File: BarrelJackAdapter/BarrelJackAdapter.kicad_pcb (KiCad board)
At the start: 2 copper layers, 15.2 x 45.7 mm, 7 parts, among them J1 Barrel_Jack_Switch, J2 Conn_01x03, J4 Conn_01x03, U1 L7805

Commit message: wip
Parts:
- added C3: C_P1U, Capacitor_SMD:C_0603_1608Metric, F.Cu at (163.0, 52.1)
- added C4: C_22U_1210, Capacitor_SMD:C_1210_3225Metric, F.Cu at (155.6, 43.2)
- added C5: C_22U_1210, Capacitor_SMD:C_1210_3225Metric, F.Cu at (148.8, 52.9)
- added L1: L_4p7U_13p5A, Inductor_SMD:L_Coilcraft_XxL4040, F.Cu at (155.8, 50.7)
- added R1: R_49p9K, Resistor_SMD:R_0603_1608Metric, F.Cu at (163.0, 54.6)
- added R2: R_10K, Resistor_SMD:R_0603_1608Metric, F.Cu at (163.0, 57.1)
- C1: value 0.33u -> C_10U_805; footprint Capacitor_SMD:C_0603_1608Metric -> Capacitor_SMD:C_0805_2012Metric
- C2: value 0.1u -> C_P1U
- U1: value L7805 -> TPS563207DRLR; footprint Package_TO_SOT_SMD:TO-263-2 -> Package_TO_SOT_SMD:SOT-563
- moved C1 30.5 mm to (153.9, 56.4), turned to -90 degrees
- moved C2 29.2 mm to (163.0, 49.6), turned to 0 degrees
- moved U1 27.8 mm to (158.0, 56.6), turned to 0 degrees
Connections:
- C2 pad 1: +5V -> +9V
- U1 pad 2: GND -> Net-(U1-SW)
- U1 pad 3: +5V -> GND
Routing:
- net GND: vias 66 -> 0
- removed copper zone on F.Cu, net +5V
- removed copper zone on F.Cu, net +9V
- removed copper zone on F.Cu, net GND

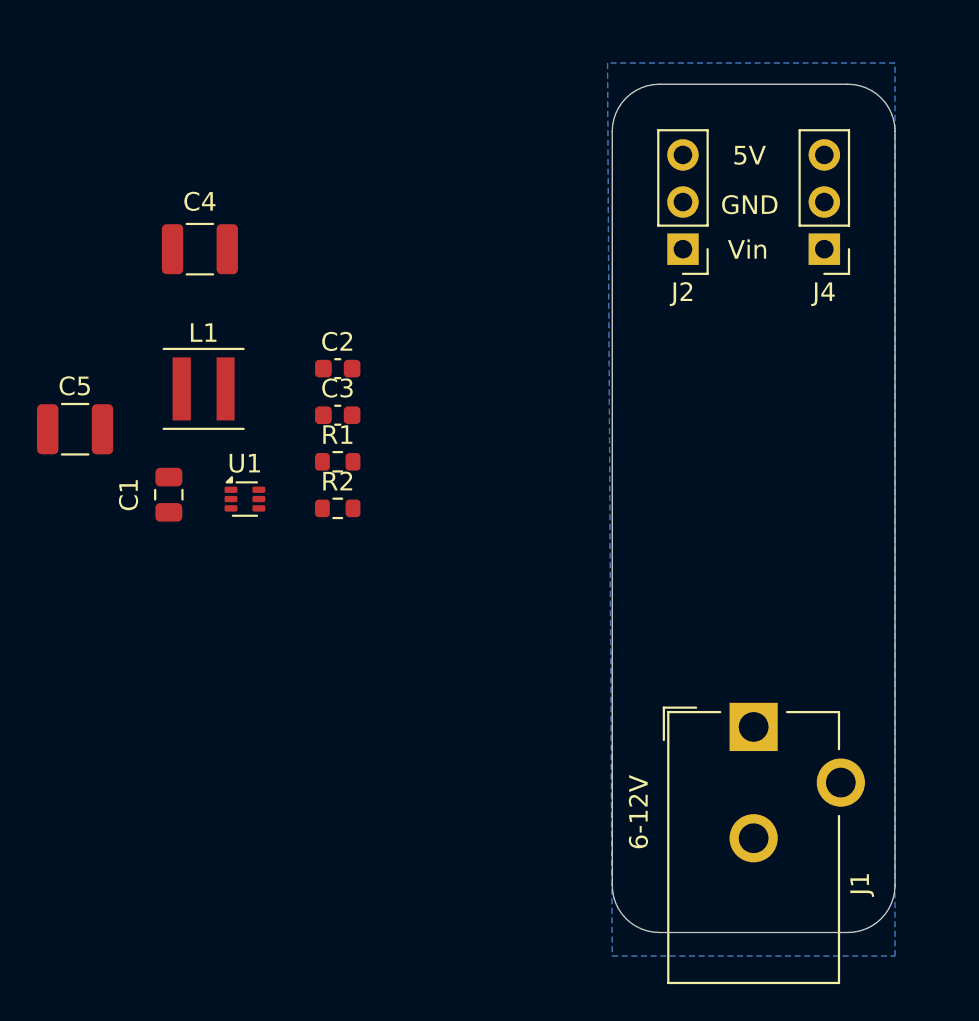
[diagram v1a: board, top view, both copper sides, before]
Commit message: first rev of buck converter based version.
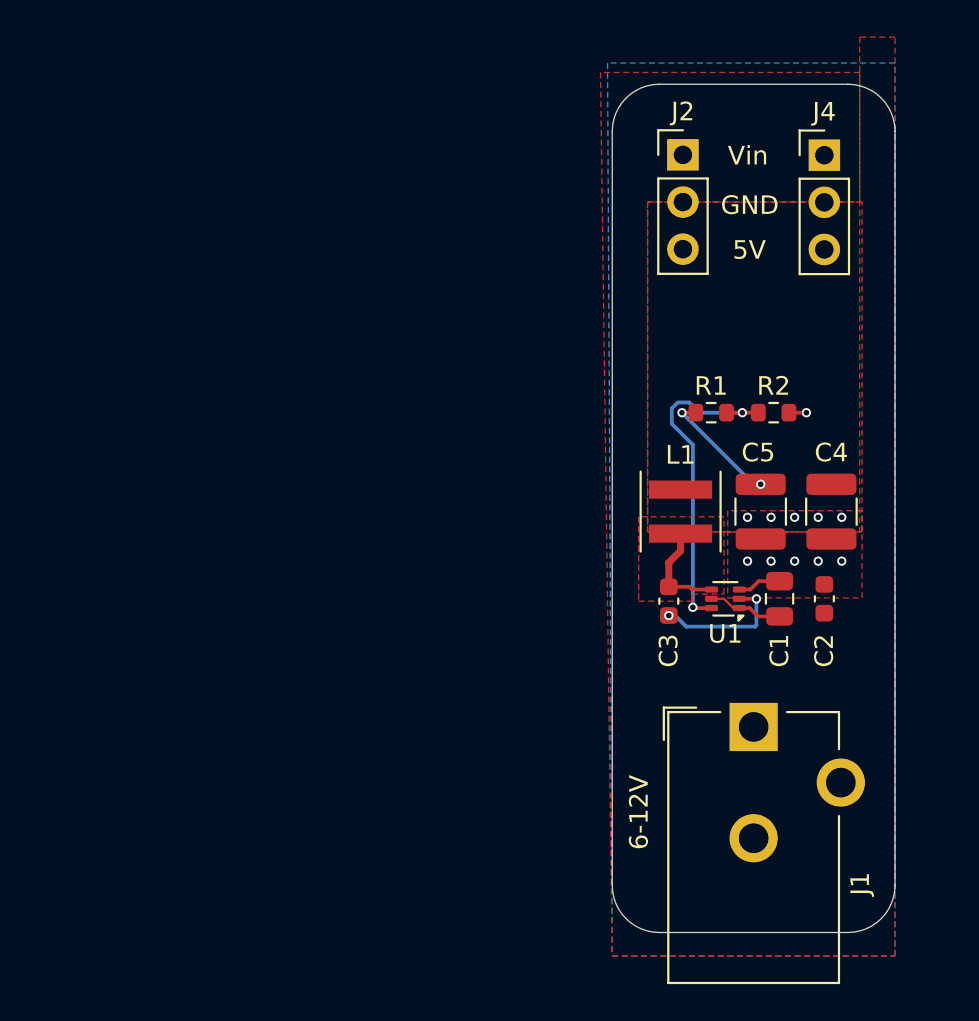
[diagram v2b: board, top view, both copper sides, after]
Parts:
- moved C5 37.2 mm to (185.8, 57.3), turned to -90 degrees
- moved C4 36.9 mm to (189.6, 57.3), turned to -90 degrees
- moved C1 33.4 mm to (186.8, 62.0), turned to 90 degrees
- moved C2 29.0 mm to (189.2, 62.0), turned to 90 degrees
- moved L1 26.5 mm to (181.5, 57.3), turned to 90 degrees
- moved U1 26.4 mm to (183.9, 62.0), turned to 180 degrees
- moved R2 24.1 mm to (186.5, 52.0)
- moved C3 20.5 mm to (180.8, 62.2), turned to -90 degrees
- moved R1 20.3 mm to (183.1, 52.0)
- moved J2 5.08 mm to (181.6, 38.1), turned to 0 degrees
- moved J4 5.06 mm to (189.2, 38.1), turned to 0 degrees
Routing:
- net Net-(U1-FB): track 0.00 -> 18.1 mm, vias 0 -> 2
- net Net-(U1-SW): track 0.00 -> 7.43 mm, vias 0 -> 2
- net +5V: track 0.00 -> 6.59 mm, vias 0 -> 2
- net Net-(U1-BST): track 0.00 -> 5.51 mm
- net +9V: track 0.00 -> 4.06 mm
- net GND: track 0.00 -> 3.30 mm, vias 0 -> 11
- added copper zone on F.Cu, net +5V
- added copper zone on F.Cu, net +9V
- added copper zone on F.Cu, net GND
- added copper zone on F.Cu, net Net-(U1-BST)
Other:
- copper layers 2 -> 4

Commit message: add 3.3v LDO
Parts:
- added C6: C_4p7U, Capacitor_SMD:C_0603_1608Metric, F.Cu at (188.1, 48.8)
- added U2: LDL212PV33R, Package_DFN_QFN:DFN-6-1EP_2x2mm_P0.65mm_EP1x1.6mm, F.Cu at (184.2, 49.1)
- J2, J4: value Conn_01x03 -> Conn_01x04; footprint Connector_PinHeader_2.54mm:PinHeader_1x03_P2.54mm_Vertical -> Connector_PinHeader_2.54mm:PinHeader_1x04_P2.54mm_Vertical
- moved G*** 3.81 mm to (185.4, 53.3)
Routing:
- net +3.3V: track 0.00 -> 16.0 mm
- net +5V: track 6.59 -> 9.84 mm
- net GND: track 3.30 -> 4.28 mm, vias 11 -> 13

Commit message: Remove some vias to the back ground plane.
Localize the high current loop to Front Copper.

Move the switch node connection to Cu2 - sandwich
between clean ground pours.
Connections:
- net Net-(U1-BST) renamed /BST
- net Net-(U1-FB) renamed /FB
- net Net-(U1-SW) renamed /SW
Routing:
- net GND: vias 13 -> 11
- added copper zone on B.Cu, net +9V
- added copper zone on In1.Cu, net GND
- added copper zone on In2.Cu, net GND
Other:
- board text added: "3.3V"
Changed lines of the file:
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@@
 	(net 2 "+9V")
 	(net 3 "+5V")
-	(net 4 "Net-(U1-SW)")
-	(net 5 "Net-(U1-BST)")
-	(net 6 "Net-(U1-FB)")
+	(net 4 "/SW")
+	(net 5 "/BST")
+	(net 6 "/FB")
 	(net 7 "+3.3V")
 	(net 8 "unconnected-(U2-NC-Pad5)")
@@
 			(layers "F.Cu" "F.Paste" "F.Mask")
 			(roundrect_rratio 0.25)
-			(net 4 "Net-(U1-SW)")
+			(net 4 "/SW")
 			(pinfunction "SW")
 			(pintype "output")
@@
 			(layers "F.Cu" "F.Paste" "F.Mask")
 			(roundrect_rratio 0.25)
-			(net 5 "Net-(U1-BST)")
+			(net 5 "/BST")
 			(pinfunction "BST")
 			(pintype "output")
@@
 			(layers "F.Cu" "F.Paste" "F.Mask")
 			(roundrect_rratio 0.25)
-			(net 6 "Net-(U1-FB)")
+			(net 6 "/FB")
 			(pinfunction "FB")
 			(pintype "input")
@@
 		(tags "DFN 0.65")
 		(property "Reference" "U2"
-			(at 3.302 -0.146 360)
+			(at 3.302 -0.146 0)
 			(layer "F.SilkS")
 			(effects
@@
 		)
 		(property "Value" "LDL212PV33R"
-			(at 0 2.025 360)
+			(at 0 2.025 0)
 			(layer "F.Fab")
 			(effects
@@
 		)
 		(fp_text user "${REFERENCE}"
-			(at 0 0 360)
+			(at 0 0 0)
 			(layer "F.Fab")
 			(effects
@@
 			(layers "F.Cu" "F.Paste" "F.Mask")
 			(roundrect_rratio 0.25)
-			(net 5 "Net-(U1-BST)")
+			(net 5 "/BST")
 			(pintype "passive")
 		)
@@
 			(layers "F.Cu" "F.Paste" "F.Mask")
 			(roundrect_rratio 0.25)
-			(net 4 "Net-(U1-SW)")
+			(net 4 "/SW")
 			(pintype "passive")
 		)
@@
 			(layers "F.Cu" "F.Paste" "F.Mask")
 			(roundrect_rratio 0.25)
-			(net 6 "Net-(U1-FB)")
+			(net 6 "/FB")
 			(pintype "passive")
 		)
@@
 		(tags "capacitor")
 		(property "Reference" "C6"
-			(at 3.035 0 360)
+			(at 3.035 0 0)
 			(layer "F.SilkS")
 			(effects
@@
 		)
 		(property "Value" "C_4p7U"
-			(at 0 1.43 360)
+			(at 0 1.43 0)
 			(layer "F.Fab")
 			(effects
@@
 		)
 		(fp_text user "${REFERENCE}"
-			(at 0 0 360)
+			(at 0 0 0)
 			(layer "F.Fab")
 			(effects
@@
 			(layers "F.Cu" "F.Paste" "F.Mask")
 			(roundrect_rratio 0.25)
-			(net 6 "Net-(U1-FB)")
+			(net 6 "/FB")
 			(pintype "passive")
 		)
@@
 			(size 0.98 3.4)
 			(layers "F.Cu" "F.Paste" "F.Mask")
-			(net 5 "Net-(U1-BST)")
+			(net 5 "/BST")
 			(pinfunction "1")
 			(pintype "passive")
@@
 		)
 	)
+	(gr_text "3.3V"
+		(at 183.769 46.355 0)
+		(layer "F.SilkS")
+		(effects
+			(font
+				(size 1 1)
+				(thickness 0.15)
+			)
+			(justify left bottom)
+		)
+	)
 	(gr_text "Vin"
 		(at 184.023 38.735 0)
@@
 	)
 	(via
-		(at 186.3598 57.6326)
-		(size 0.5)
-		(drill 0.3)
+		(at 184.15 49.149)
+		(size 0.35)
+		(drill 0.2)
 		(layers "F.Cu" "B.Cu")
-		(free yes)
 		(net 1)
 	)
 	(via
-		(at 188.8998 59.9948)
+		(at 186.3598 57.6326)
 		(size 0.5)
 		(drill 0.3)
@@
 	)
 	(via
-		(at 185.0898 59.9948)
-		(size 0.5)
-		(drill 0.3)
+		(at 184.15 48.641)
+		(size 0.35)
+		(drill 0.2)
 		(layers "F.Cu" "B.Cu")
-		(free yes)
 		(net 1)
 	)
@@
 	)
 	(via
-		(at 186.3598 59.9948)
-		(size 0.5)
-		(drill 0.3)
-		(layers "F.Cu" "B.Cu")
-		(free yes)
-		(net 1)
-	)
-	(via
-		(at 190.1698 59.9948)
-		(size 0.5)
-		(drill 0.3)
-		(layers "F.Cu" "B.Cu")
-		(free yes)
-		(net 1)
-	)
-	(via
 		(at 190.1698 57.6326)
 		(size 0.5)
@@
 	)
 	(via
-		(at 187.6298 59.9948)
+		(at 188.8998 57.6326)
 		(size 0.5)
 		(drill 0.3)
@@
 	)
 	(via
-		(at 188.8998 57.6326)
-		(size 0.5)
-		(drill 0.3)
+		(at 184.15 49.657)
+		(size 0.35)
+		(drill 0.2)
 		(layers "F.Cu" "B.Cu")
-		(free yes)
 		(net 1)
 	)
@@
 		(end 185.801 55.851)
 		(width 0.2)
-		(layer "B.Cu")
+		(layer "In2.Cu")
 		(net 3)
 	)
@@
 		(end 185.4164 55.851)
 		(width 0.2)
-		(layer "B.Cu")
+		(layer "In2.Cu")
 		(net 3)
 	)
@@
 		(end 185.4962 63.5254)
 		(width 0.2)
-		(layer "B.Cu")
+		(layer "In2.Cu")
 		(net 4)
 	)
@@
 		(end 181.7878 63.5254)
 		(width 0.2)
-		(layer "B.Cu")
+		(layer "In2.Cu")
 		(net 4)
 	)
@@
 		(end 185.5724 63.4492)
 		(width 0.2)
-		(layer "B.Cu")
+		(layer "In2.Cu")
 		(net 4)
 	)
@@
 		(end 180.848 62.927)
 		(width 0.2)
-		(layer "B.Cu")
+		(layer "In2.Cu")
 		(net 4)
 	)
@@
 		(end 181.1894 62.927)
 		(width 0.2)
-		(layer "B.Cu")
+		(layer "In2.Cu")
 		(net 4)
 	)
@@
 		(end 181.0092 52.5868)
 		(width 0.2)
-		(layer "B.Cu")
+		(layer "In2.Cu")
 		(net 6)
 	)
@@
 		(end 182.499 51.9938)
 		(width 0.2)
-		(layer "B.Cu")
+		(layer "In2.Cu")
 		(net 6)
 	)
@@
 		(end 181.331382 51.4438)
 		(width 0.2)
-		(layer "B.Cu")
+		(layer "In2.Cu")
 		(net 6)
 	)
@@
 		(end 182.1434 53.721)
 		(width 0.2)
-		(layer "B.Cu")
+		(layer "In2.Cu")
 		(net 6)
 	)
@@
 		(end 181.949 51.4438)
 		(width 0.2)
-		(layer "B.Cu")
+		(layer "In2.Cu")
 		(net 6)
 	)
@@
 		(end 182.0799 53.6575)
 		(width 0.2)
-		(layer "B.Cu")
+		(layer "In2.Cu")
 		(net 6)
 	)
@@
 		(end 182.0926 51.5874)
 		(width 0.2)
-		(layer "B.Cu")
+		(layer "In2.Cu")
 		(net 6)
 	)
@@
 		(end 181.0092 51.765982)
 		(width 0.2)
-		(layer "B.Cu")
+		(layer "In2.Cu")
 		(net 6)
 	)
@@
 		(end 182.0799 53.6575)
 		(width 0.2)
-		(layer "B.Cu")
+		(layer "In2.Cu")
 		(net 6)
 	)
@@
 	)
 	(zone
-		(net 2)
-		(net_name "+9V")
-		(layer "F.Cu")
-		(hatch edge 0.5)
-		(connect_pads thru_hole_only
-			(clearance 0.5)
-		)
-		(min_thickness 0.25)
-		(filled_areas_thickness no)
-		(fill yes
-			(thermal_gap 0.5)
-			(thermal_bridge_width 0.5)
-		)
-		(polygon
-			(pts
-				(xy 191.135 31.75) (xy 191.135 58.42) (xy 179.705 58.42) (xy 179.705 40.64) (xy 191.135 40.64) (xy 191.135 33.655)
-				(xy 177.165 33.655) (xy 177.8 81.28) (xy 193.04 81.28) (xy 193.04 31.75)
-			)
-		)
-	)
-	(zone
 		(net 3)
 		(net_name "+5V")
@@
 		(priority 1)
 		(connect_pads thru_hole_only
-			(clearance 0.5)
+			(clearance 0.25)
 		)
-		(min_thickness 0.25)
+		(min_thickness 0.2)
 		(filled_areas_thickness no)
 		(fill yes
@@
 	(zone
 		(net 5)
-		(net_name "Net-(U1-BST)")
+		(net_name "/BST")
 		(layer "F.Cu")
 		(hatch edge 0.5)
 		(priority 3)
 		(connect_pads thru_hole_only
-			(clearance 0.5)
+			(clearance 0.25)
 		)
-		(min_thickness 0.25)
+		(min_thickness 0.2)
 		(filled_areas_thickness no)
 		(fill yes
@@
 	)
 	(zone
+		(net 2)
+		(net_name "+9V")
+		(layers "F&B.Cu")
+		(hatch edge 0.5)
+		(connect_pads thru_hole_only
+			(clearance 0.25)
+		)
+		(min_thickness 0.2)
+		(filled_areas_thickness no)
+		(fill yes
+			(thermal_gap 0.5)
+			(thermal_bridge_width 0.5)
+		)
+		(polygon
+			(pts
+				(xy 191.135 31.75) (xy 191.135 58.42) (xy 179.705 58.42) (xy 179.705 40.64) (xy 191.135 40.64) (xy 191.135 33.655)
+				(xy 177.165 33.655) (xy 177.8 81.28) (xy 193.04 81.28) (xy 193.04 31.75)
+			)
+		)
+	)
+	(zone
 		(net 1)
 		(net_name "GND")
-		(layer "B.Cu")
+		(layers "In1.Cu" "In2.Cu" "B.Cu")
 		(hatch edge 0.5)
 		(priority 2)

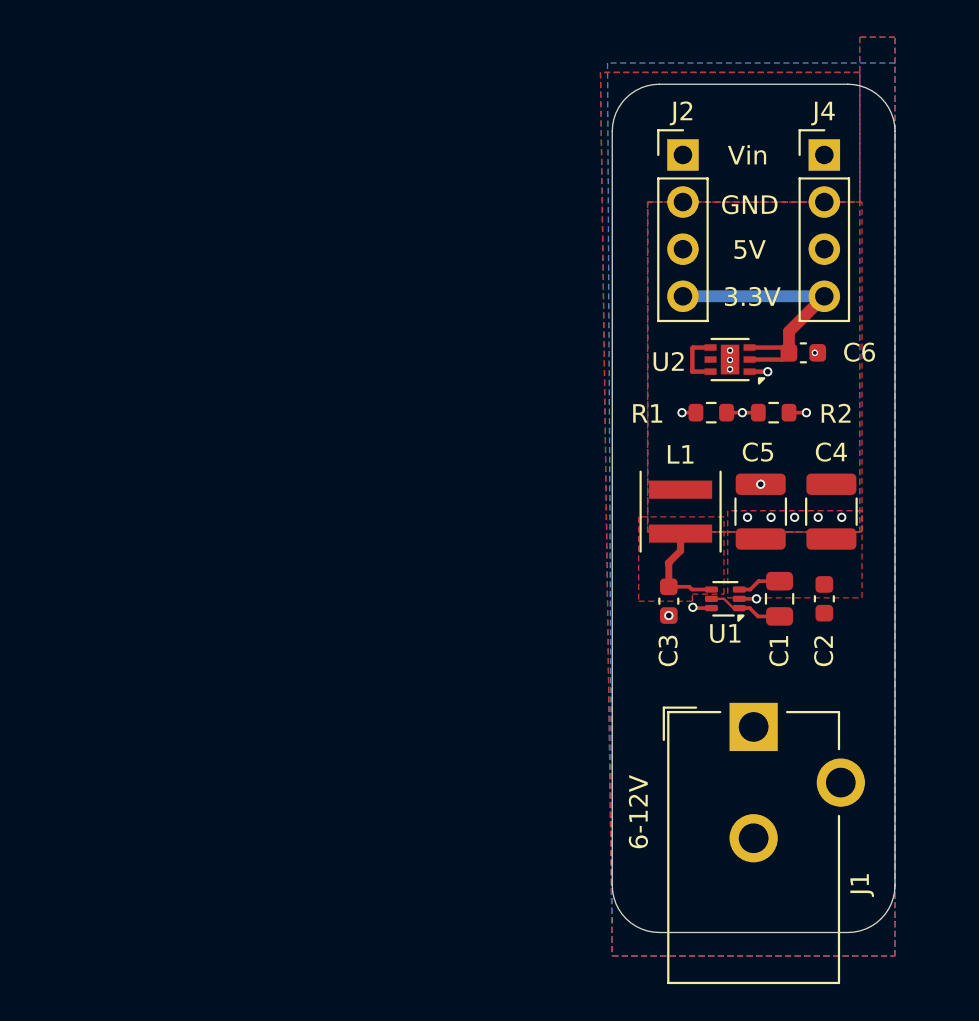
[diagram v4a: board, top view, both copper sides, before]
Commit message: Fix schematic.
Better Layout

Close #2
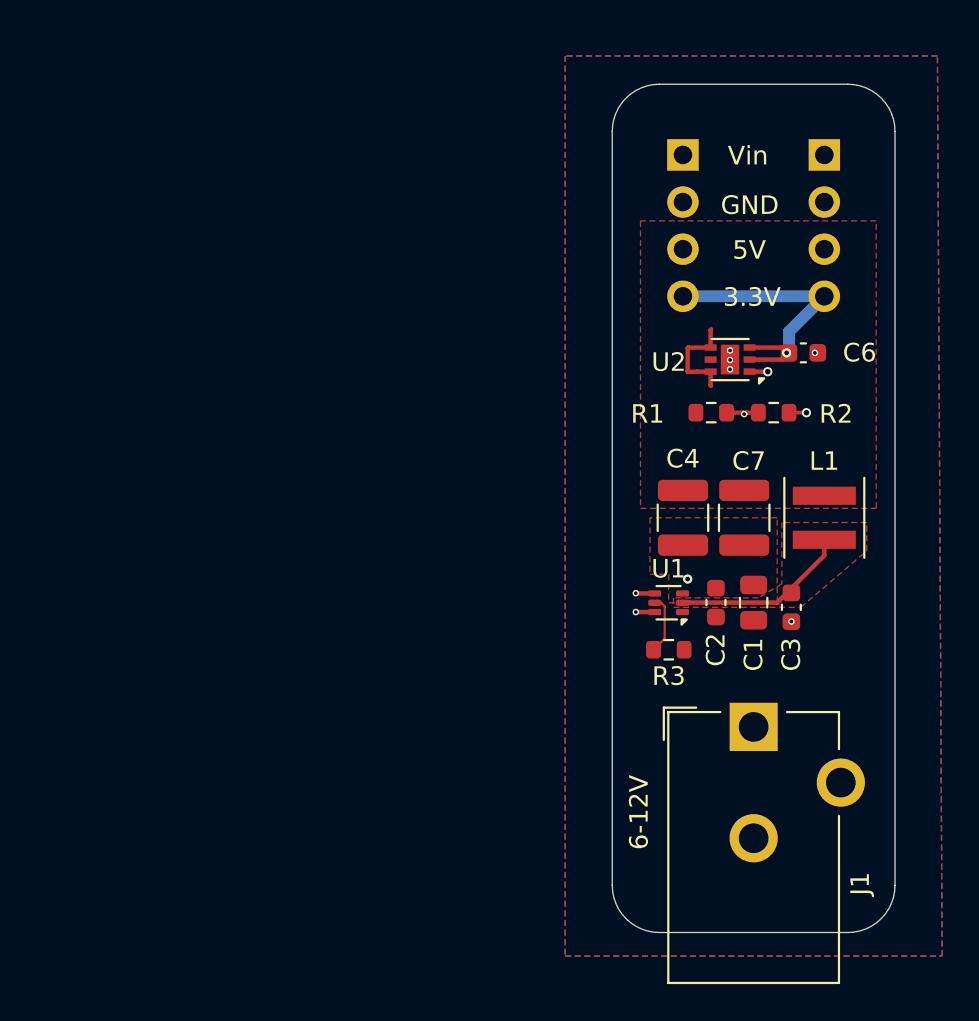
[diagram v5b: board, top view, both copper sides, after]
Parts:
- removed C5: C_22U_1210, Capacitor_SMD:C_1210_3225Metric
- added C7: C_22U_1210, Capacitor_SMD:C_1210_3225Metric, F.Cu at (184.9, 57.7)
- added R3: R_10K, Resistor_SMD:R_0603_1608Metric, F.Cu at (180.8, 64.8)
- J2, J4: moved to B.Cu
- L1: value L_4p7U_13p5A -> L_10U_1A
- moved C4 8.01 mm to (181.6, 57.7)
- moved L1 7.75 mm to (189.2, 57.7)
- moved C3 6.61 mm to (187.5, 62.5), turned to 90 degrees
- moved C2 5.85 mm to (183.4, 62.2)
- moved U1 3.07 mm to (180.8, 62.2)
- moved G*** 1.48 mm to (186.7, 52.6)
- moved C1 1.41 mm to (185.4, 62.2)
- turned J2 to 180 degrees
- turned J4 to 180 degrees
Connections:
- L1 pad 1: /BST -> /SW
- U1 pad 5: +9V -> Net-(U1-EN)
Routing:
- net /BST: track 5.51 -> 10.1 mm, vias 0 -> 2
- net +5V: track 9.84 -> 5.53 mm, vias 2 -> 0
- net +9V: track 4.06 -> 0.00 mm
- net Net-(U1-EN): track 0.00 -> 3.21 mm
- net GND: track 4.28 -> 1.93 mm, vias 11 -> 7
- net /SW: track 7.43 -> 9.55 mm, vias 2 -> 0
- net /FB: track 18.1 -> 16.6 mm
- net +3.3V: track 16.0 -> 16.1 mm, vias 0 -> 1
- added copper zone on In1.Cu, net +9V
- added copper zone on F.Cu, net /SW
- removed copper zone on B.Cu, net +9V
- removed copper zone on F.Cu, net /BST
- removed copper zone on In1.Cu, net GND
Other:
- board text added: "Barrel Jack Adapter.V1.1Buck Copyright 2024 Tad Truex"
- board text removed: "Barrel Jack Adapter. Copyright 2024 Tad Truex"
